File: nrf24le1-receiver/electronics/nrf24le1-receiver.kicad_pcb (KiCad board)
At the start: 2 copper layers, 19 x 25 mm, 19 parts, among them K1 CONN_3, K2 CONN_3, K3 CONN_3, K4 CONN_3, P1 CONN_1, P2 CONN_1, P3 CONN_1, SW1 BIND, U1 MCP1703, U2 NRF24LE1

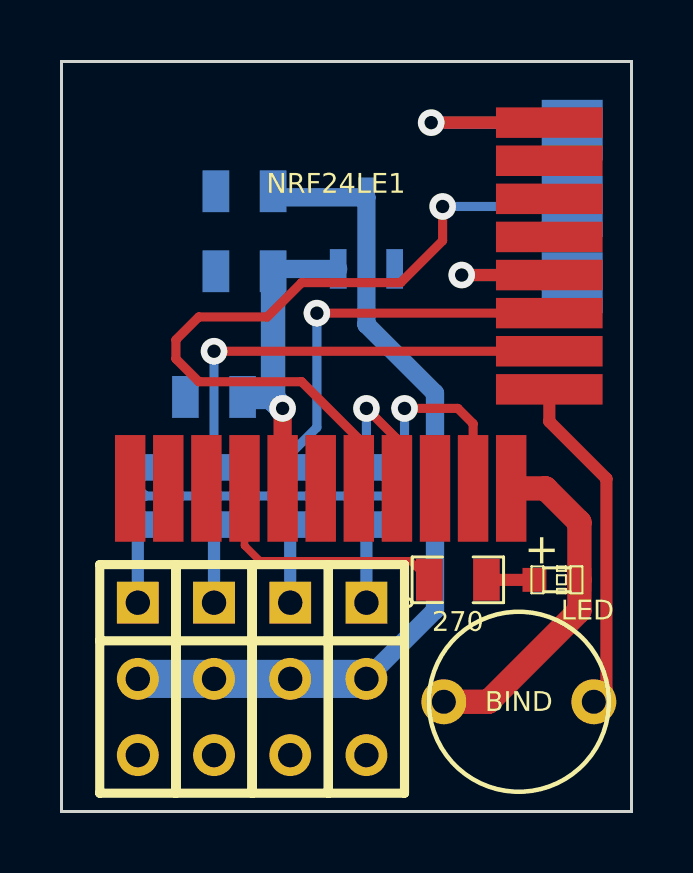
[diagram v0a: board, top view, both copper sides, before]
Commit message: Add 2x 47uF 0805 tantalum bypass cap to combat brown-outs
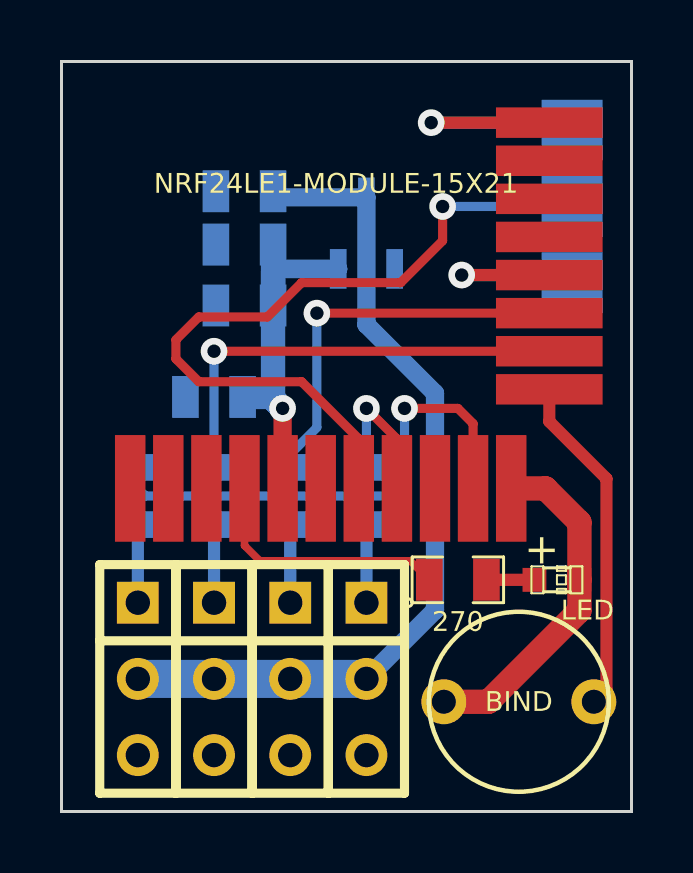
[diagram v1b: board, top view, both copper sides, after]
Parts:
- added C4: 47uF, SM0805, B.Cu at (38.1, 56.1)
- C1: value 10u -> 47uF
- U2: value NRF24LE1 -> NRF24LE1-MODULE-15X21
- moved C3 0.89 mm to (38.1, 54.1)
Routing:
- net +3.3V: track 11.1 -> 16.2 mm
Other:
- board text added: "Rev 2"
- board text removed: "Rev 1"
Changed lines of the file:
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@@
 (kicad_pcb (version 3) (host pcbnew "(2013-jul-07)-stable")
   (general
-    (links 32)
+    (links 34)
     (no_connects 0)
     (area 31.949999 41.072999 51.531533 73.8124)
     (thickness 1.6)
     (drawings 15)
-    (tracks 80)
+    (tracks 83)
     (zones 0)
-    (modules 19)
+    (modules 20)
     (nets 18)
   )
@@
   )
   (setup
-    (last_trace_width 0.254)
+    (last_trace_width 0.6096)
     (user_trace_width 0.2032)
     (user_trace_width 0.254)
@@
     (pad_to_mask_clearance 0)
     (aux_axis_origin 32 73)
-    (visible_elements 7FFFFFBF)
+    (visible_elements 7FFFFFAF)
     (pcbplotparams
       (layerselection 3178497)
@@
   (net 11 /TX)
   (net 12 N-0000010)
-  (net 13 N-0000011)
+  (net 13 N-0000025)
   (net 14 N-000003)
   (net 15 N-000008)
@@
     (add_net /TX)
     (add_net N-0000010)
-    (add_net N-0000011)
+    (add_net N-0000025)
     (add_net N-000003)
     (add_net N-000008)
@@
   )
   (module SM0805   placed (layer B.Cu)
-    (at 38.1 54.991 180)
+    (at 38.1 54.102 180)
     (attr smd)
     (fp_text reference C3 (at 0 0.3175 180) (layer B.SilkS) hide
@@
       (effects (font (size 0.50038 0.50038) (thickness 0.10922)) (justify mirror))
     )
-    (fp_text value 10u (at 2.667 0 180) (layer B.SilkS)
+    (fp_text value 47uF (at 2.921 0 180) (layer B.SilkS)
       (effects (font (size 0.6604 0.6604) (thickness 0.1524)) (justify mirror))
     )
@@
     (pad 2 smd rect (at 0.9525 0 270) (size 0.889 1.397)
       (layers B.Cu B.Paste B.Mask)
-      (net 13 N-0000011)
+      (net 14 N-000003)
     )
     (model smd/chip_cms.wrl
@@
     (pad 2 smd rect (at 0.9525 0) (size 0.889 1.397)
       (layers F.Cu F.Paste F.Mask)
-      (net 14 N-000003)
+      (net 13 N-0000025)
     )
     (model smd/chip_cms.wrl
@@
     (pad 1 thru_hole rect (at -2.54 0 270) (size 1.397 1.397) (drill 0.8128)
       (layers *.Cu *.Mask F.SilkS)
-      (net 13 N-0000011)
+      (net 14 N-000003)
     )
     (pad 2 thru_hole circle (at 0 0 270) (size 1.397 1.397) (drill 0.8128)
@@
     (pad 1 smd rect (at -0.7493 0) (size 0.79756 0.79756)
       (layers F.Cu F.Paste F.Mask)
-      (net 14 N-000003)
+      (net 13 N-0000025)
     )
     (pad 2 smd rect (at 0.7493 0) (size 0.79756 0.79756)
@@
       (effects (font (size 1 1) (thickness 0.15)))
     )
-    (fp_text value NRF24LE1 (at 7.874 -10.16) (layer F.SilkS)
+    (fp_text value NRF24LE1-MODULE-15X21 (at 7.874 -10.16) (layer F.SilkS)
       (effects (font (size 0.6604 0.6604) (thickness 0.1524)))
     )
@@
     )
   )
+  (module SM0805 (layer B.Cu)
+    (at 38.1 56.134 180)
+    (attr smd)
+    (fp_text reference C4 (at 0.381 -2.54 180) (layer B.SilkS)
+      (effects (font (size 0.50038 0.50038) (thickness 0.10922)) (justify mirror))
+    )
+    (fp_text value 47uF (at 3.048 0 180) (layer B.SilkS)
+      (effects (font (size 0.6604 0.6604) (thickness 0.1524)) (justify mirror))
+    )
+    (fp_circle (center -1.651 -0.762) (end -1.651 -0.635) (layer B.SilkS) (width 0.09906))
+    (fp_line (start -0.508 -0.762) (end -1.524 -0.762) (layer B.SilkS) (width 0.09906))
+    (fp_line (start -1.524 -0.762) (end -1.524 0.762) (layer B.SilkS) (width 0.09906))
+    (fp_line (start -1.524 0.762) (end -0.508 0.762) (layer B.SilkS) (width 0.09906))
+    (fp_line (start 0.508 0.762) (end 1.524 0.762) (layer B.SilkS) (width 0.09906))
+    (fp_line (start 1.524 0.762) (end 1.524 -0.762) (layer B.SilkS) (width 0.09906))
+    (fp_line (start 1.524 -0.762) (end 0.508 -0.762) (layer B.SilkS) (width 0.09906))
+    (pad 1 smd rect (at -0.9525 0 180) (size 0.889 1.397)
+      (layers B.Cu B.Paste B.Mask)
+      (net 1 +3.3V)
+    )
+    (pad 2 smd rect (at 0.9525 0 180) (size 0.889 1.397)
+      (layers B.Cu B.Paste B.Mask)
+      (net 17 VSS)
+    )
+    (model smd/chip_cms.wrl
+      (at (xyz 0 0 0))
+      (scale (xyz 0.1 0.1 0.1))
+      (rotate (xyz 0 0 0))
+    )
+  )
   (gr_text + (at 48.006 64.262) (layer F.SilkS)
     (effects (font (size 1.016 1.016) (thickness 0.1778)))
@@
     (effects (font (size 0.6604 0.6604) (thickness 0.1524)) (justify left mirror))
   )
-  (gr_text "Rev 1" (at 50.038 71.628) (layer B.SilkS)
+  (gr_text "Rev 2" (at 50.038 71.628) (layer B.SilkS)
     (effects (font (size 0.8128 0.8128) (thickness 0.1524)) (justify left mirror))
   )
@@
   (gr_line (start 32 48) (end 51 48) (angle 90) (layer Edge.Cuts) (width 0.1))
   (gr_line (start 32 73) (end 32 48) (angle 90) (layer Edge.Cuts) (width 0.1))
+  (segment (start 41.2242 54.9148) (end 39.0525 54.9148) (width 0.6096) (layer B.Cu) (net 1))
+  (segment (start 39.0525 54.9148) (end 39.0525 54.102) (width 0.6096) (layer B.Cu) (net 1))
+  (segment (start 39.0525 54.102) (end 39.0525 56.134) (width 0.8128) (layer B.Cu) (net 1))
   (segment (start 38.0365 59.182) (end 38.989 59.182) (width 0.8128) (layer B.Cu) (net 1))
   (segment (start 38.989 59.182) (end 39.37 59.563) (width 0.8128) (layer B.Cu) (net 1))
@@
   (via (at 42.164 59.563) (size 0.889) (layers F.Cu B.Cu) (net 11))
   (segment (start 37.084 66.04) (end 37.084 63.4365) (width 0.4064) (layer B.Cu) (net 12) (status 30))
-  (segment (start 34.544 66.04) (end 34.544 63.4365) (width 0.4064) (layer B.Cu) (net 13) (status 30))
-  (segment (start 46.1645 65.278) (end 47.7647 65.278) (width 0.4064) (layer F.Cu) (net 14) (status 30))
+  (segment (start 46.1645 65.278) (end 47.7647 65.278) (width 0.4064) (layer F.Cu) (net 13) (status 30))
+  (segment (start 34.544 66.04) (end 34.544 63.4365) (width 0.4064) (layer B.Cu) (net 14) (status 30))
   (segment (start 42.164 66.04) (end 42.164 63.4365) (width 0.4064) (layer B.Cu) (net 15) (status 30))
   (segment (start 39.624 66.04) (end 39.624 63.4365) (width 0.4064) (layer B.Cu) (net 16) (status 30))

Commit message: Add Gerber for revision 2 PCB
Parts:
- U2: value NRF24LE1-MODULE-15X21 -> NRF24LE1
